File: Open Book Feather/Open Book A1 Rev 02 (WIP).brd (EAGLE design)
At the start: 77.5 x 112.3 mm, 127 parts, among them J1 SJ-43514-SMT, J2 10118193-0001LF, Q1 DMG341, Q2 IRLML0100, SW1 SPDT_SWITCH, U1 AP2112-3.3, U2 MCP73831T-2ACI/OT, U3 ATSAMD51J64-TQFP(10X10), U4 GD25Q16C (or GD25Q32C), U5 74AC165D, U6 GD25Q16C (or GD25Q32C), U7 23K256-I/SN, U8 MAX4466EXK+T, X1 JSTPH, X2 2x5 0.05" SWD

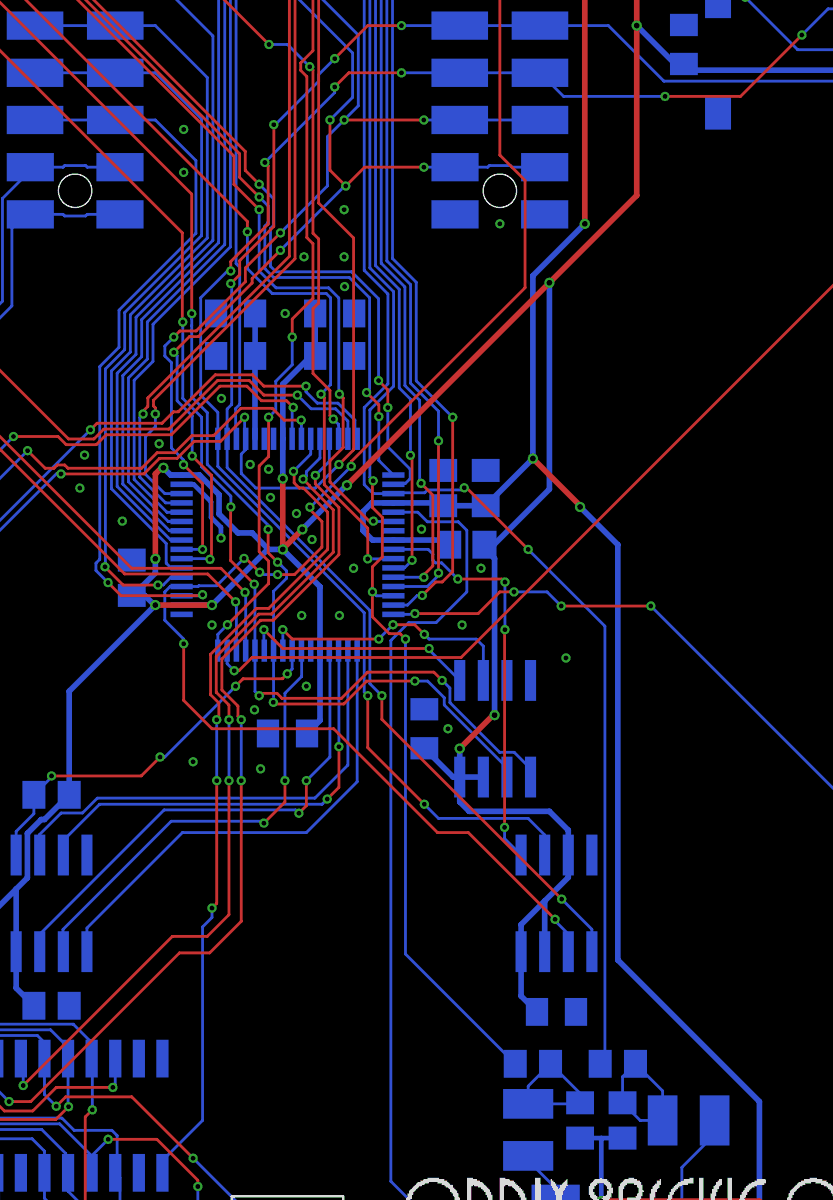
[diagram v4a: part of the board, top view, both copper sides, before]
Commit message: route card detect signal
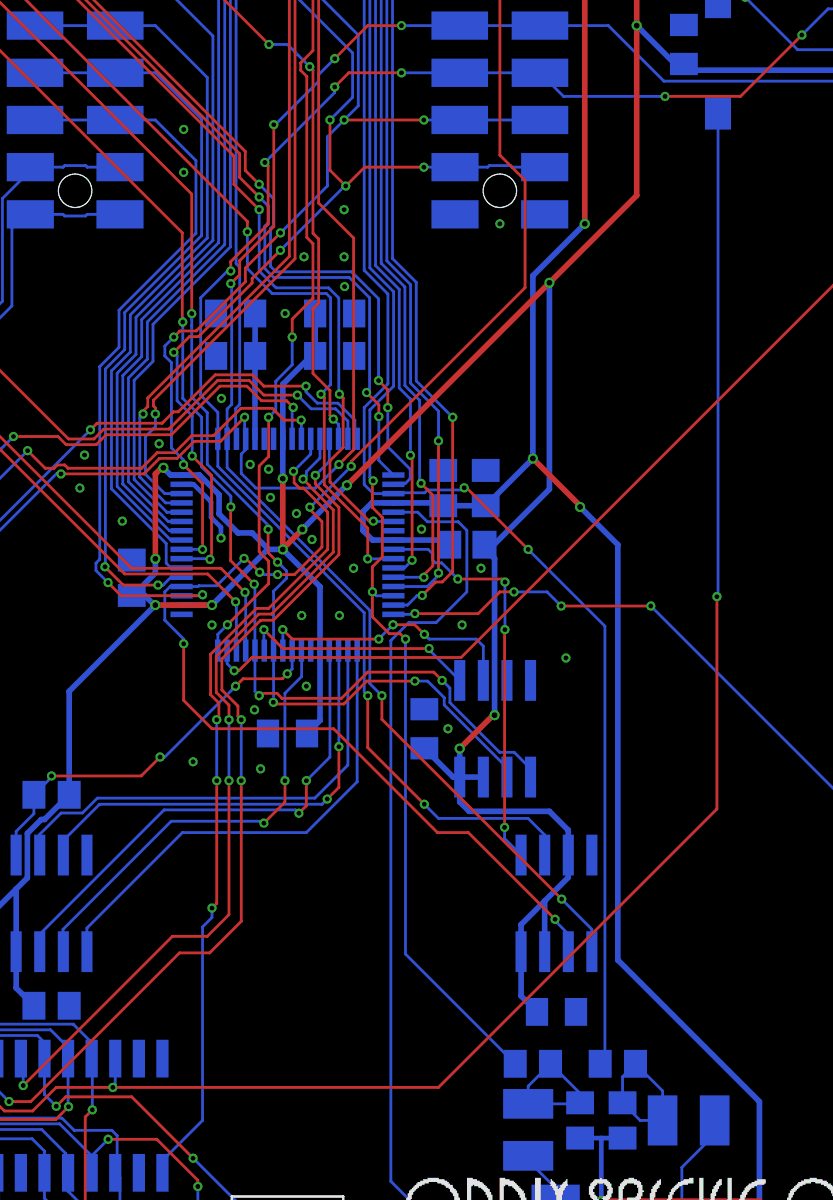
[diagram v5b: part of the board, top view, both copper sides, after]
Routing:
- net BUTTON7: track 10.6 -> 86.8 mm, vias 2 -> 3
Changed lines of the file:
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@@
 <grid distance="0.01" unitdist="inch" unit="inch" style="lines" multiple="1" display="no" altdistance="1" altunitdist="mil" altunit="inch"/>
 <layers>
-<layer number="1" name="Top" color="4" fill="1" visible="no" active="yes"/>
+<layer number="1" name="Top" color="4" fill="1" visible="yes" active="yes"/>
 <layer number="2" name="Route2" color="1" fill="3" visible="no" active="no"/>
 <layer number="3" name="Route3" color="4" fill="3" visible="no" active="no"/>
@@
 <layer number="19" name="Unrouted" color="6" fill="1" visible="yes" active="yes"/>
 <layer number="20" name="Dimension" color="15" fill="1" visible="yes" active="yes"/>
-<layer number="21" name="tPlace" color="14" fill="1" visible="no" active="yes"/>
+<layer number="21" name="tPlace" color="14" fill="1" visible="yes" active="yes"/>
 <layer number="22" name="bPlace" color="13" fill="1" visible="yes" active="yes"/>
-<layer number="23" name="tOrigins" color="15" fill="1" visible="no" active="yes"/>
+<layer number="23" name="tOrigins" color="15" fill="1" visible="yes" active="yes"/>
 <layer number="24" name="bOrigins" color="15" fill="1" visible="yes" active="yes"/>
-<layer number="25" name="tNames" color="7" fill="1" visible="no" active="yes"/>
+<layer number="25" name="tNames" color="7" fill="1" visible="yes" active="yes"/>
 <layer number="26" name="bNames" color="7" fill="1" visible="yes" active="yes"/>
 <layer number="27" name="tValues" color="7" fill="1" visible="no" active="yes"/>
@@
 <layer number="37" name="tTest" color="7" fill="1" visible="no" active="yes"/>
 <layer number="38" name="bTest" color="7" fill="1" visible="no" active="yes"/>
-<layer number="39" name="tKeepout" color="4" fill="11" visible="no" active="yes"/>
+<layer number="39" name="tKeepout" color="4" fill="11" visible="yes" active="yes"/>
 <layer number="40" name="bKeepout" color="1" fill="11" visible="yes" active="yes"/>
-<layer number="41" name="tRestrict" color="4" fill="10" visible="no" active="yes"/>
+<layer number="41" name="tRestrict" color="4" fill="10" visible="yes" active="yes"/>
 <layer number="42" name="bRestrict" color="1" fill="10" visible="yes" active="yes"/>
 <layer number="43" name="vRestrict" color="2" fill="10" visible="no" active="yes"/>
@@
 <layer number="49" name="Reference" color="7" fill="1" visible="no" active="yes"/>
 <layer number="50" name="dxf" color="7" fill="1" visible="no" active="yes"/>
-<layer number="51" name="tDocu" color="7" fill="1" visible="no" active="yes"/>
+<layer number="51" name="tDocu" color="7" fill="1" visible="yes" active="yes"/>
 <layer number="52" name="bDocu" color="7" fill="1" visible="yes" active="yes"/>
 <layer number="53" name="tGND_GNDA" color="7" fill="9" visible="no" active="no"/>
@@
 <wire x1="29.464" y1="20.828" x2="26.416" y2="20.828" width="0.1524" layer="1"/>
 <contactref element="MICROSD" pad="CD2"/>
-<wire x1="29.591" y1="22.3774" x2="62.035" y2="73.28" width="0" layer="19" extent="16-16"/>
+<wire x1="62.035" y1="73.28" x2="62.035" y2="47.303" width="0.1524" layer="16"/>
+<wire x1="62.035" y1="47.303" x2="61.976" y2="47.244" width="0.1524" layer="16"/>
+<via x="61.976" y="47.244" extent="1-16" drill="0.254"/>
+<wire x1="61.976" y1="47.244" x2="61.976" y2="35.814" width="0.1524" layer="1"/>
+<wire x1="46.99" y1="20.828" x2="29.464" y2="20.828" width="0.1524" layer="1"/>
+<wire x1="61.976" y1="35.814" x2="46.99" y2="20.828" width="0.1524" layer="1"/>
 </signal>
 <signal name="A7_MIC">

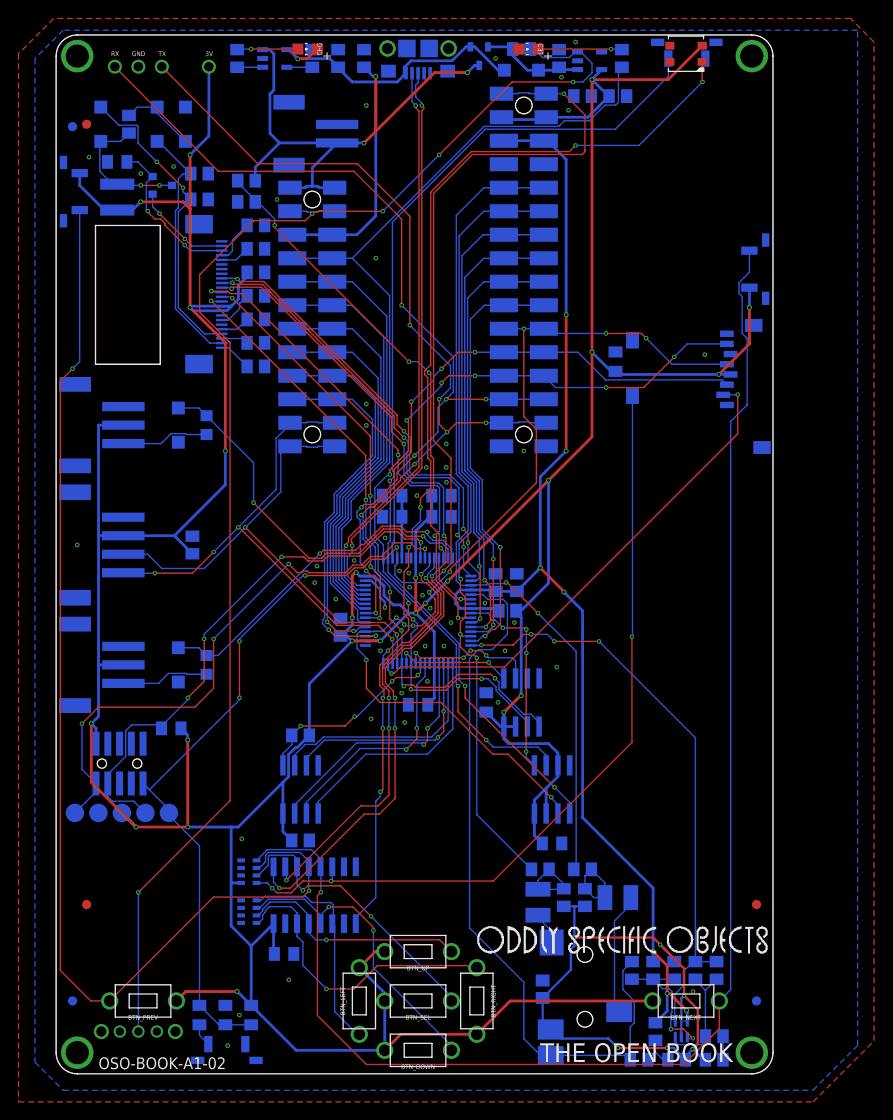
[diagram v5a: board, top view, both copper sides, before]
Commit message: move leds to bottom, improve placement
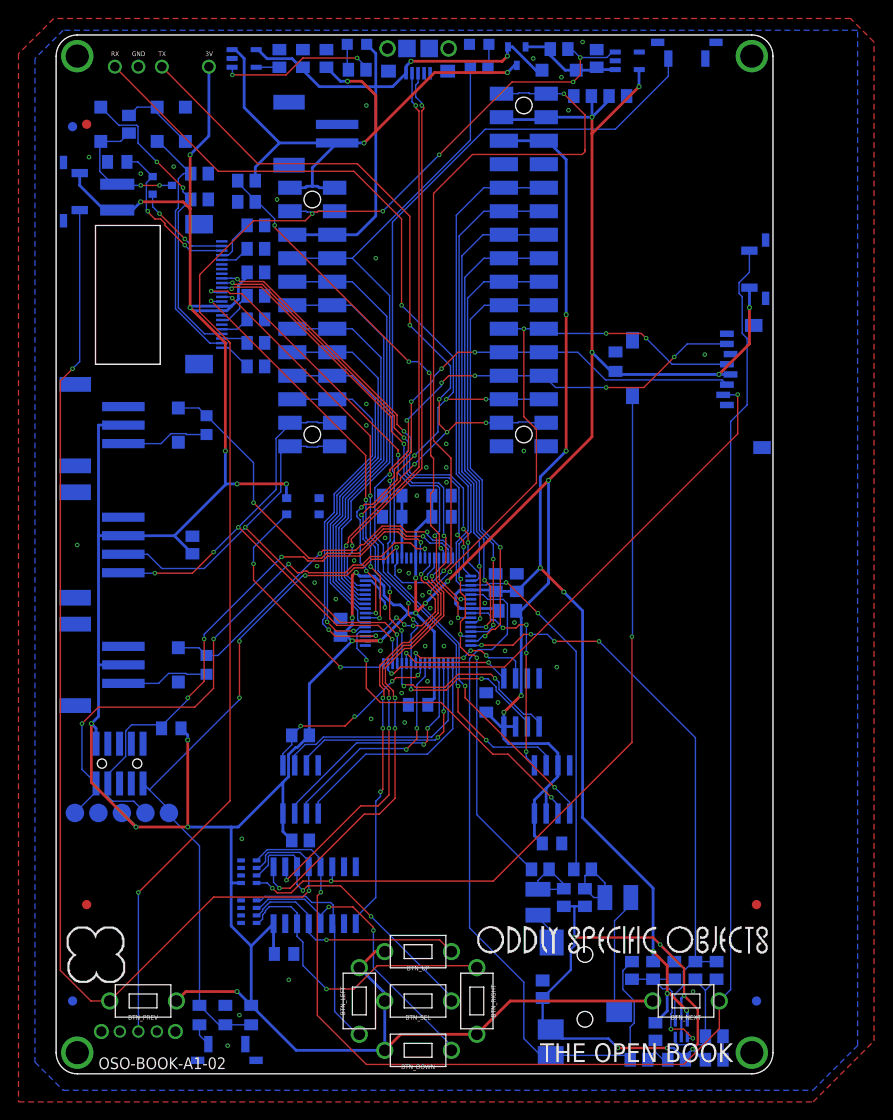
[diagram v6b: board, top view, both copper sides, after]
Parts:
- moved STATUS 64.1 mm to (26.4, 61.3), flipped to the bottom
- moved U$44 55.2 mm to (4.06, 12.9), flipped to the top
- moved R8 15.4 mm to (45.5, 108.8), turned to 180 degrees
- moved R4 13.0 mm to (32.3, 108.5), turned to 180 degrees
- moved CHG 5.36 mm to (32.3, 111.3), flipped to the bottom, turned to 270 degrees
- moved LED 5.36 mm to (45.5, 111.3), flipped to the bottom, turned to 270 degrees
- moved C4 4.06 mm to (29.0, 109.7)
- moved C1 4.06 mm to (58.2, 109.7)
- moved D1 4.06 mm to (54.1, 108.5)
- moved Q1 4.06 mm to (49.5, 110.0)
- moved R1 4.06 mm to (54.1, 110.7)
- moved U1 4.06 mm to (61.5, 109.5)
- moved R2 3.81 mm to (26.4, 109.7)
- moved R3 3.56 mm to (23.9, 109.7)
- moved U2 3.30 mm to (20.1, 109.7)
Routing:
- net D8_NEOPIX: track 90.5 -> 26.7 mm, vias 5 -> 2
- net N$5: track 2.76 -> 16.7 mm, vias 0 -> 2
- net D13: track 87.9 -> 74.1 mm
- net VBUS: track 55.3 -> 65.4 mm, vias 1 -> 2
- net VBAT: track 60.2 -> 67.9 mm
- net N$7: track 9.06 -> 2.51 mm, vias 1 -> 0
- net +3V3: track 535.8 -> 530.7 mm, vias 24 -> 27
- net N$4: track 6.60 -> 2.80 mm, vias 1 -> 0
- net EN: track 152.6 -> 150.0 mm, vias 5 -> 6
- net UNIFONT_CS: track 22.0 -> 22.6 mm
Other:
- board text added: "A Neopixel on D8 (PA15)."
- board text removed: "A thru-hole Neopixel (D8) is useful to show CircuitPython status, or you can use it for general blinkenlights."
- board text removed: "R8: current limiting for LED #13"

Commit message: improved silkscreen documentation
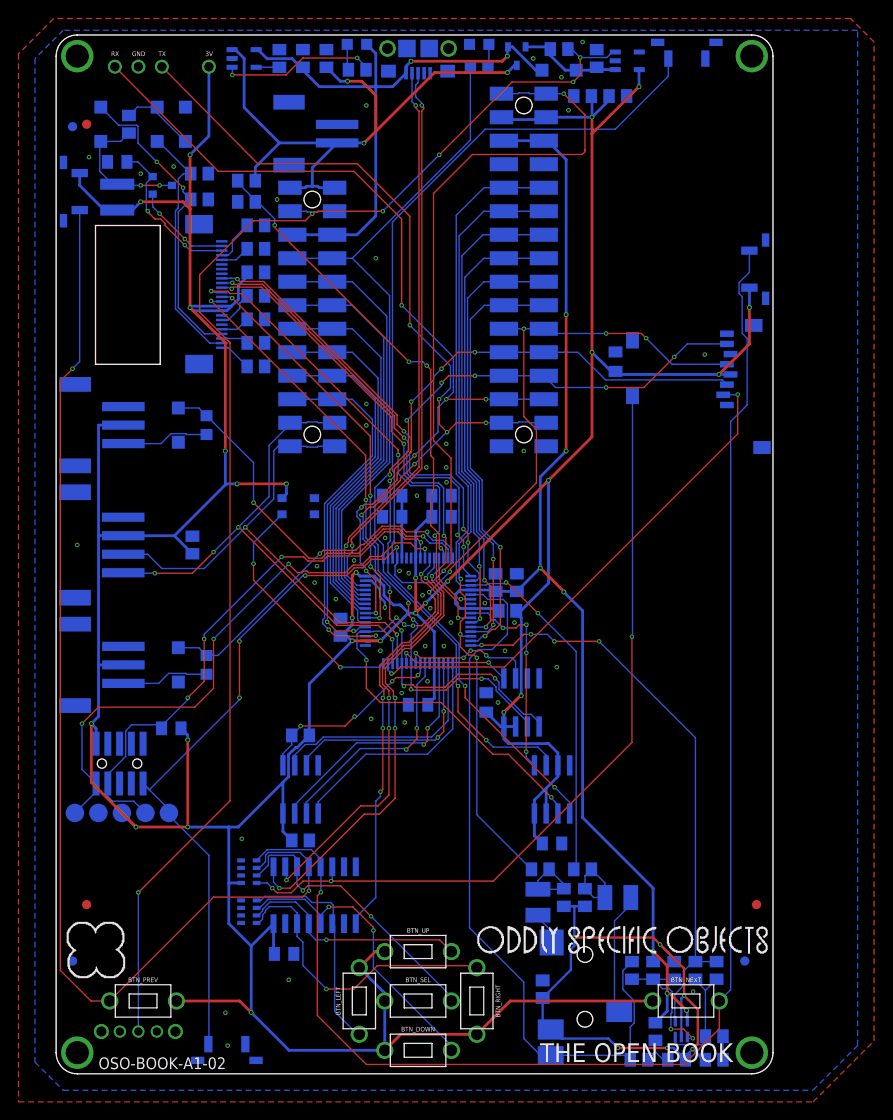
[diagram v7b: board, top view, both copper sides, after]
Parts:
- removed C13: 0.1uF, microbuilder:0805_10MGAP
- removed R6: 10K, microbuilder:0805_10MGAP
- removed R7: 100, microbuilder:0805_10MGAP
- moved FID1 4.50 mm to (74.2, 12.2)
- moved FID5 4.32 mm to (1.52, 12.2)
- moved STATUS 0.51 mm to (25.9, 61.3)
- moved U$44 0.51 mm to (4.06, 13.4)
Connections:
- removed net N$1: BTN_RESET.P$2, R7.1
- net !RESET: now also BTN_RESET.P$2; no longer C13.2, R6.2, R7.2
- net +3V3: no longer R6.1
- net GND: no longer C13.1
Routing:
- net N$1: track 2.49 -> 0.00 mm
- net !RESET: track 158.7 -> 156.9 mm
- net SDA: track 55.8 -> 56.4 mm
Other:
- board text added: "A0 PA02"
- board text added: "A0/PA02: R audio out A1/PA05: L audio out A7/PB04: Raw mic in"
- board text added: "A1 PA05"
- board text added: "A2 PB08"
- board text added: "A3 PB09"
- board text added: "A4 PA04"
- board text added: "A5 PA06"
- board text added: "AREF PA03"
- board text added: "Amplified mic signal on A10/PA07"
- board text added: "Bits: 0: LEFT 1: DOWN 2: UP 3: RIGHT 4: SEL 5: PREV 6: NEXT 7: SD Card Detect"
- board text added: "Clock: D48/PB31 Data: D49/PB30 Latch: D50/PB00"
- board text added: "D1&Q1 conspire to let only the higher of VBAT & VBUS reach 3.3V regulator U1. C1 filters regulator input; C2 & C3 filter output. R1 pulls EN high to keep the regulator on. BATTERY: U2 is a LiPo charging controller. Powered by VBUS, it charges the battery at a rate determined by R3. C4=filter for VBAT, R4 limits current to CHG LED. R14 & R15: a voltage divider for VBAT to make a battery gauge on A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"
- board text added: "D10 PA20"
- board text added: "D11 PA21"
- board text added: "D12 PA22"
- board text added: "D13 PA23"
- board text added: "D5 PA16"
- board text added: "D6 PA18"
- board text added: "D9 PA19"
- board text added: "Lots to unpack here. For starters, the Feather pinout is mostly identical to the Adafruit SAMD51 boards you're familiar with, PWM & analog pins where you expect them (minus "extra" pin D4). SERCOM0: Serial (RX/TX = D0/D1 = PB17/PB16) SERCOM1: SPI (MOSI/MISO/SCK = D27/D26/D28 = PB23/PB22/PA17) SERCOM2: I²C (SDA/SCL = D24/D25 = PA12/PA13) SERCOM4: SPI for the display: MOSI1/MISO1/SCK1 = D41/D43/D42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"
- board text added: "MISO PB22"
- board text added: "MOSI PB23"
- board text added: "Optional 23K256 SRAM chip U7 provides a buffer for the display. It uses the e-paper screen's SPI interface on SERCOM4. Chip select SRCS is D53/PB14."
- board text added: "Pins: ECS=D44/PB07 EDC =D45/PB05 ERST=D46 /PA00 EBSY=D47/PA01"
- board text added: "R1 up top pulls EN high. Switching SW1 pulls EN low, disabling power supply U1 along with most of the board."
- board text added: "R6 pulls reset high. BTN_RESET pulls it low. Double-tap to enter UF2 bootloader."
- board text added: "RESET BUTTON"
- board text added: "RX PB17"
- board text added: "SCK PA17"
- board text added: "SCL PA13"
- board text added: "SDA PA12"
- board text added: "TX PB16"
- board text added: "The Open Book by Joey Castillo @josecastillo. Based in large part on @Adafruit's great open source designs. OSO logo & lazer bear by Joseph Devens, @DoctorDevens. Thanks to Tom F, Josh L, Brent R & many others. Made with . in Brooklyn & Texas."
- board text added: "U4 is another GD25Q16C Flash chip on a dedicated QSPI bus (D35-D40/PA08-PA11 & PB10- PB11). It's the CIRCUITPY drive that shows up when you plug it in! R9 pulls U4's CS high; the microcontroller can drive it low (active) via QSPI_CS (D36)."
- board text added: "U5 is a 74165 8-bit shift register. It takes the state of 7 of the board's buttons (L/D/U/R /Sel/Prev/Next) and fits them in a single byte."
- board text added: "U6 is a GD25Q16C Flash memory chip on the main SPI bus (BCS: D52/PB06). Stores Unicode character data and Unifont glyphs for every code point in the Basic Multliingual Plane. Contents covered by GPL with font embedding exception."
- board text added: "U8 is a MAX4466 amp for an inline electret mic."
- board text added: "Uses the main SPI bus (MISO, MOSI, SCK). SDCS is D4/PA14."
- board text removed: "...clock D48, data D49 & latch D50. Lock also on D51."
- board text removed: "A0"
- board text removed: "A0: Right audio out A1: Left audio out A7: Raw mic in"
- board text removed: "A3"
- board text removed: "A4"
- board text removed: "A5"
- board text removed: "AREF"
- board text removed: "Bits: 0: LEFT 1: DOWN 2: UP 3: RIGHT 4: SEL 5: PREV 6: NEXT 7:"
- board text removed: "D1&Q1 conspire to let only the higher of VBAT & VBUS reach 3.3V regulator U1. C1 filters regulator input; C2 & C3 filter output. R1 pulls EN high to keep the regulator on. BATTERY: U2 is a LiPo charging controller. Powered by VBUS, it charges the battery at a rate determined by R3. C4=filter for VBAT, R4 limits current to CHG LED. R14 & R15: a voltage divider for VBAT to make a battery gauge on p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"
- board text removed: "D10"
- board text removed: "D11"
- board text removed: "D12"
- board text removed: "D13"
- board text removed: "D5"
- board text removed: "D6"
- board text removed: "D9"
- board text removed: "FFC connector: 24 pos 0.5mm pitch R/A with contacts on TOP."
- board text removed: "Lots to unpack here. For starters, the Feather header: it's a mostly identical pinout to the Adafruit SAMD51 boards you're familiar with, PWM and analog pins where you expect them (minus the "extra" pin D4). SD and Babel share the main SPI bus. Screen gets its own SPI on SERCOM4 (D41-D43), and also uses: ECS (44), EDC (45), ERST(46), and EBUSY(47). Other peripherals: * status pixel on D8 * button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"
- board text removed: "MISO"
- board text removed: "MOSI"
- board text removed: "Optional 23K256 SRAM chip U7 provides a buffer for the display. It uses the e-paper screen's SPI interface on SERCOM4. Chip select SRCS is D53."
- board text removed: "R1 up top pulls EN high. SW1 pulls EN low when switched, disabling 3V power supply U1 along with most of the board."
- board text removed: "R6 pulls reset high. BTN_RESET pulls it low. C13 is a filter cap and R7 limits current spike as C13 discharges."
- board text removed: "RESET SWITCH"
- board text removed: "SCK"
- board text removed: "The Open Book by Joey Castillo @josecastillo. Based in large part on @Adafruit's great open source designs. OSO logo & lazer bear by Joseph Devens, @DoctorDevens. Thanks to Tom F, Josh L, Brent R & many others. Made with . in Brooklyn & Texas"
- board text removed: "U4 is another GD25Q16C Flash chip, this tied to the SAMD51's dedicated QSPI bus (D35-D40); it's the CIRCUITPY drive that shows up when you plug it in! R9 pulls U4's CS high; the microcontroller can drive it low (active) via QSPI_CS (D36)."
- board text removed: "U5 is a 74165 8-bit shift register. It takes the state of the board's 8 buttons (L/D/U/R/Sel/ Prev/Next/Lock) and fits them in a single byte that we can read via.."
- board text removed: "U6 is a GD25Q16C Flash memory chip on the main SPI bus (CS: D52). It stores Unicode character data and Unifont glyphs for every code point in the Basic Multliingual Plane. Contents covered by GPL with font embedding exception."
- board text removed: "U8 is a MAX4466 amp for an inline electret mic. A10: louder mic in."
- board text removed: "Uses the main SPI bus (MISO, MOSI, SCK). Chip select is D4."
